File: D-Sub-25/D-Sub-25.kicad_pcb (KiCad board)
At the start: 2 copper layers, 82.6 x 82.6 mm, 3 parts, among them J1 Pins, J2 Socket, J3 Breakout

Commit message: Corerect URL.
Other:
- board text added: "D-Sub 25 Breakout Board ©2025 Dieter Baron github.com/T-Pau/Connector-Breakout-Boards"
- board text removed: "D-Sub 25 Breakout Board ©2025 Dieter Baron github.com/T-Pau/Breakout-Boards"

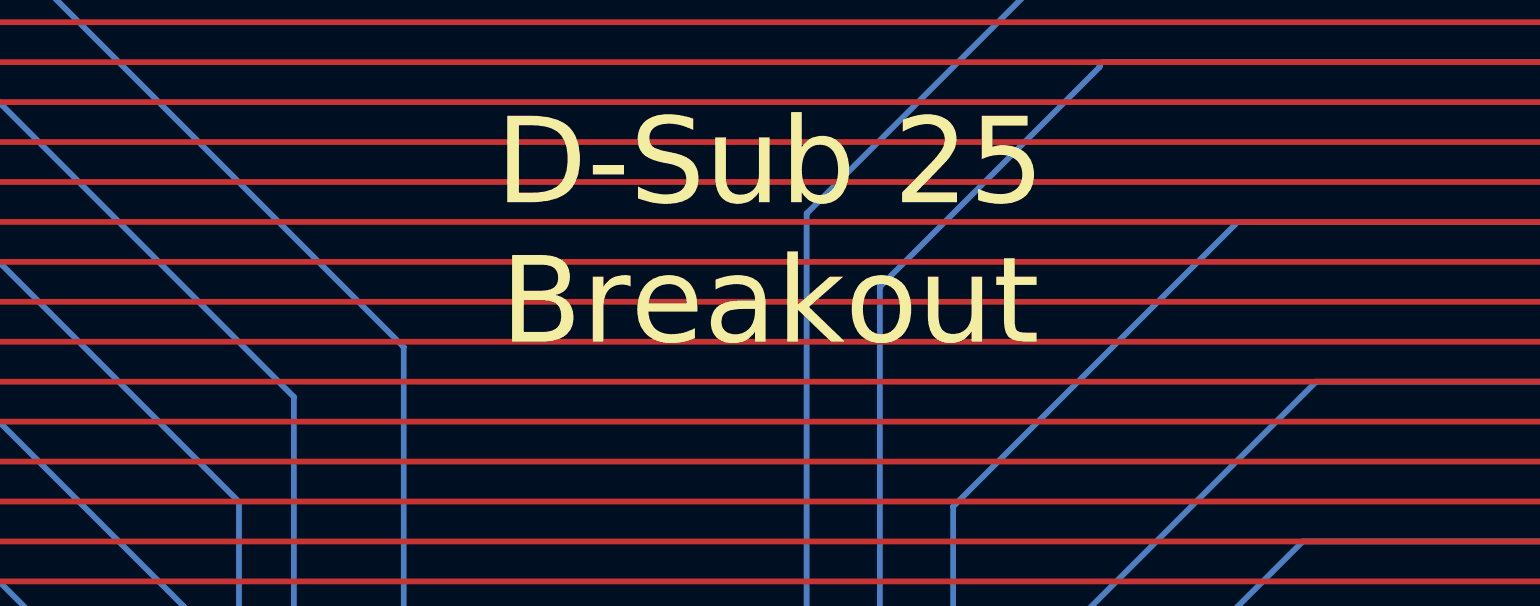
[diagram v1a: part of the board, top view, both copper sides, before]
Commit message: Improve layouts, add DIN-8 270° board.
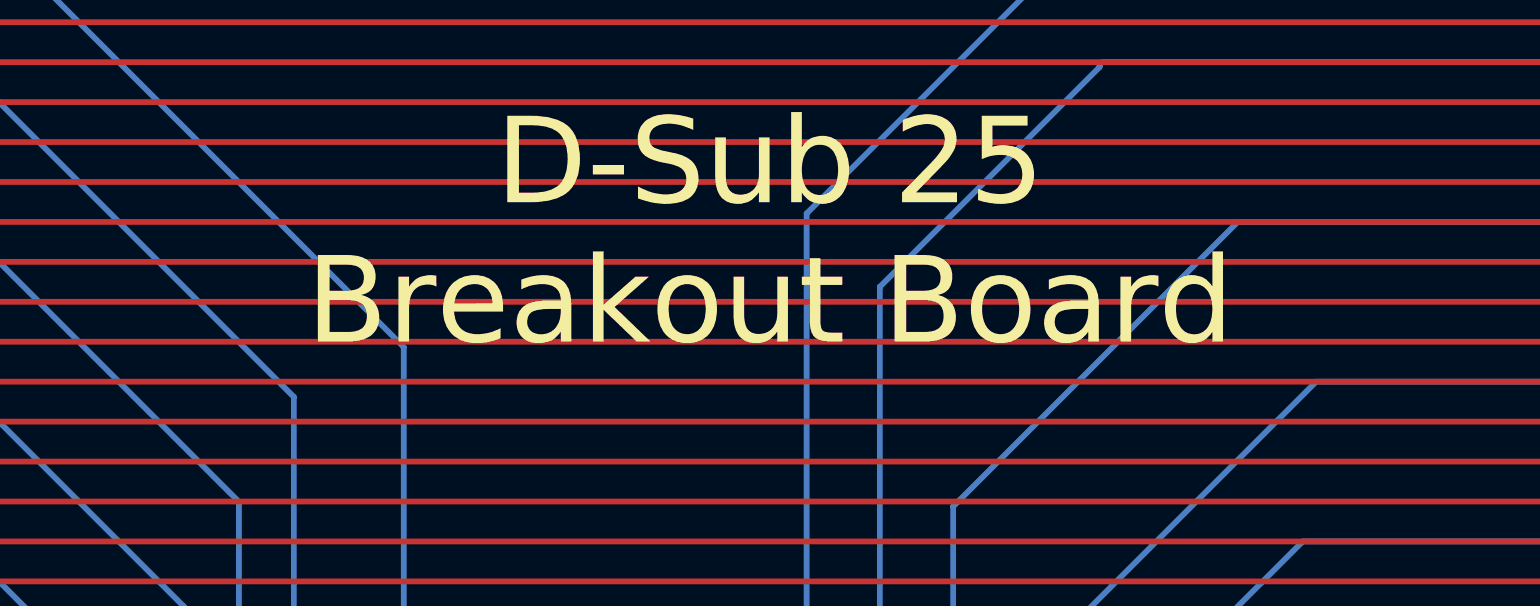
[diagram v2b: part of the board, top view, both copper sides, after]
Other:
- board text added: "D-Sub 25 Breakout Board"
- board text removed: "D-Sub 25 Breakout"

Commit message: Begin SCART breakout board.
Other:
- board text added: "D-Sub 25 Breakout Board Revision 1 ©2025 Dieter Baron github.com/T-Pau/Connector-Breakout-Boards"
- board text removed: "D-Sub 25 Breakout Board ©2025 Dieter Baron github.com/T-Pau/Connector-Breakout-Boards"
